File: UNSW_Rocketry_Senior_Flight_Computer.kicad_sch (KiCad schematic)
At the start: 21 parts, among them U1 STM32L452RETx, Y1 8MHz

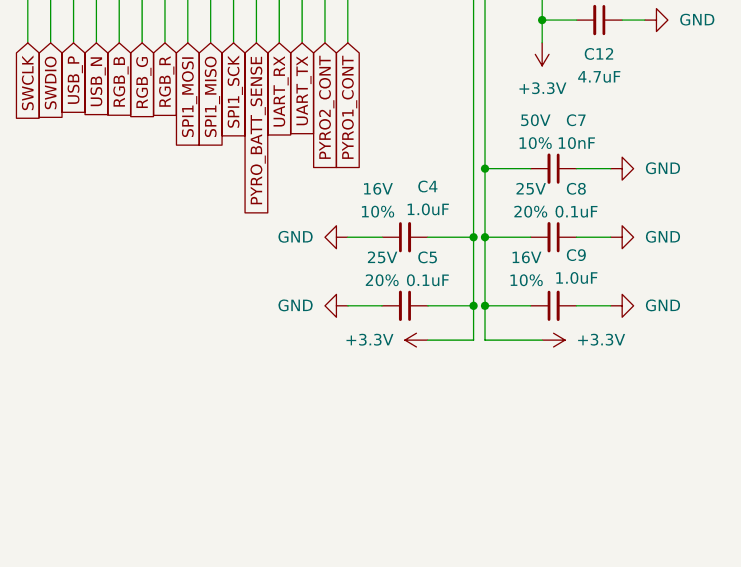
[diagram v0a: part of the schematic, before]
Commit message: chore: save working flight computer state as v0.0 baseline
Final known-good state of the senior FC before splitting into versioned
revisions (v0.0 frozen, v1.0 for the next revision).

Co-Authored-By: Claude Opus 4.7 (1M context) <noreply@anthropic.com>
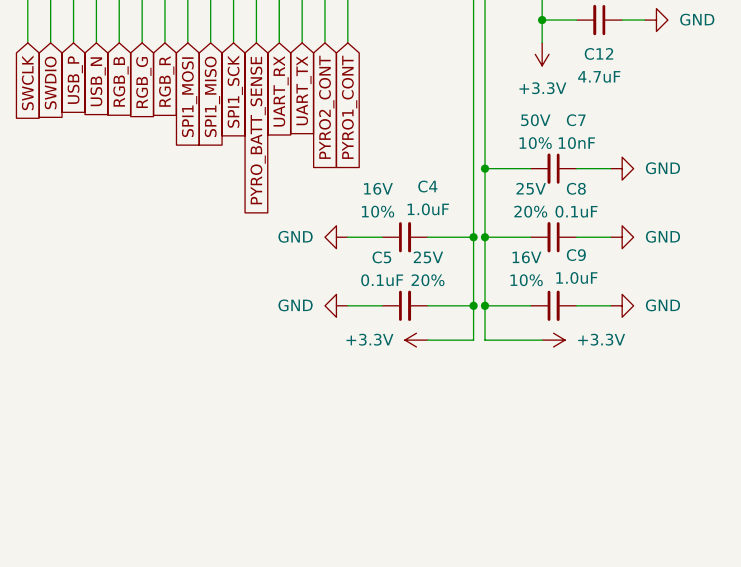
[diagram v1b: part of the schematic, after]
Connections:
- net +3.3V: now also C5.2; no longer C5.1
- net GND: now also C5.1; no longer C5.2
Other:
- moved on the sheet: C5
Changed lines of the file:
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@@
 	(symbol
 		(lib_id "PCM_SparkFun-Capacitor:0.1uF_0603_25V_20%")
-		(at 182.88 142.24 270)
+		(at 182.88 142.24 90)
+		(mirror x)
 		(unit 1)
 		(body_style 1)
@@
 		(dnp no)
 		(property "Reference" "C5"
-			(at 185.42 136.906 90)
+			(at 180.34 136.906 90)
 			(show_name no)
 			(do_not_autoplace no)
@@
 		)
 		(property "Value" "0.1uF"
-			(at 185.42 139.446 90)
+			(at 180.34 139.446 90)
 			(show_name no)
 			(do_not_autoplace no)
@@
 		)
 		(property "Footprint" "PCM_SparkFun-Capacitor:C_0603_1608Metric"
-			(at 171.45 142.24 0)
+			(at 194.31 142.24 0)
 			(hide yes)
 			(show_name no)
@@
 		)
 		(property "Datasheet" "https://cdn.sparkfun.com/assets/8/a/4/a/5/Kemet_Capacitor_Datasheet.pdf"
-			(at 168.91 142.24 0)
+			(at 196.85 142.24 0)
 			(hide yes)
 			(show_name no)
@@
 		)
 		(property "Description" "Unpolarized capacitor"
-			(at 163.83 142.24 0)
+			(at 201.93 142.24 0)
 			(hide yes)
 			(show_name no)
@@
 		)
 		(property "PROD_ID" "CAP-00810"
-			(at 166.37 142.24 0)
+			(at 199.39 142.24 0)
 			(hide yes)
 			(show_name no)
@@
 		)
 		(property "Voltage" "25V"
-			(at 180.3336 136.906 90)
+			(at 185.4264 136.906 90)
 			(show_name no)
 			(do_not_autoplace no)
@@
 		)
 		(property "Tolerance" "20%"
-			(at 180.3336 139.446 90)
+			(at 185.4264 139.446 90)
 			(show_name no)
 			(do_not_autoplace no)
